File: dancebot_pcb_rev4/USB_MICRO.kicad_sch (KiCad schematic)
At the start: 10 parts, among them IC1 CP2102N-A02-GQFN28R, J12 USB_B_Micro

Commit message: schematic ready for review!
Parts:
- J12: footprint Connector_USB:USB_Micro-B_Wuerth_629105150521 -> Connector_USB:USB_Micro-B_Amphenol_10118193-0002LF_Horizontal
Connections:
- net +3V3: now also C11.1
- net D+: no longer D303.1 (K), IC1.5 (D-), J12.2 (D-)
- new net D-: D303.1 (K), IC1.5 (D-), J12.2 (D-)
- no-connect marks 16 -> 17
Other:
- note added: "Hierarchical Labels"
- moved on the sheet: C10, C11, D1, D3, D303, IC1, J12, R12, R7, R8

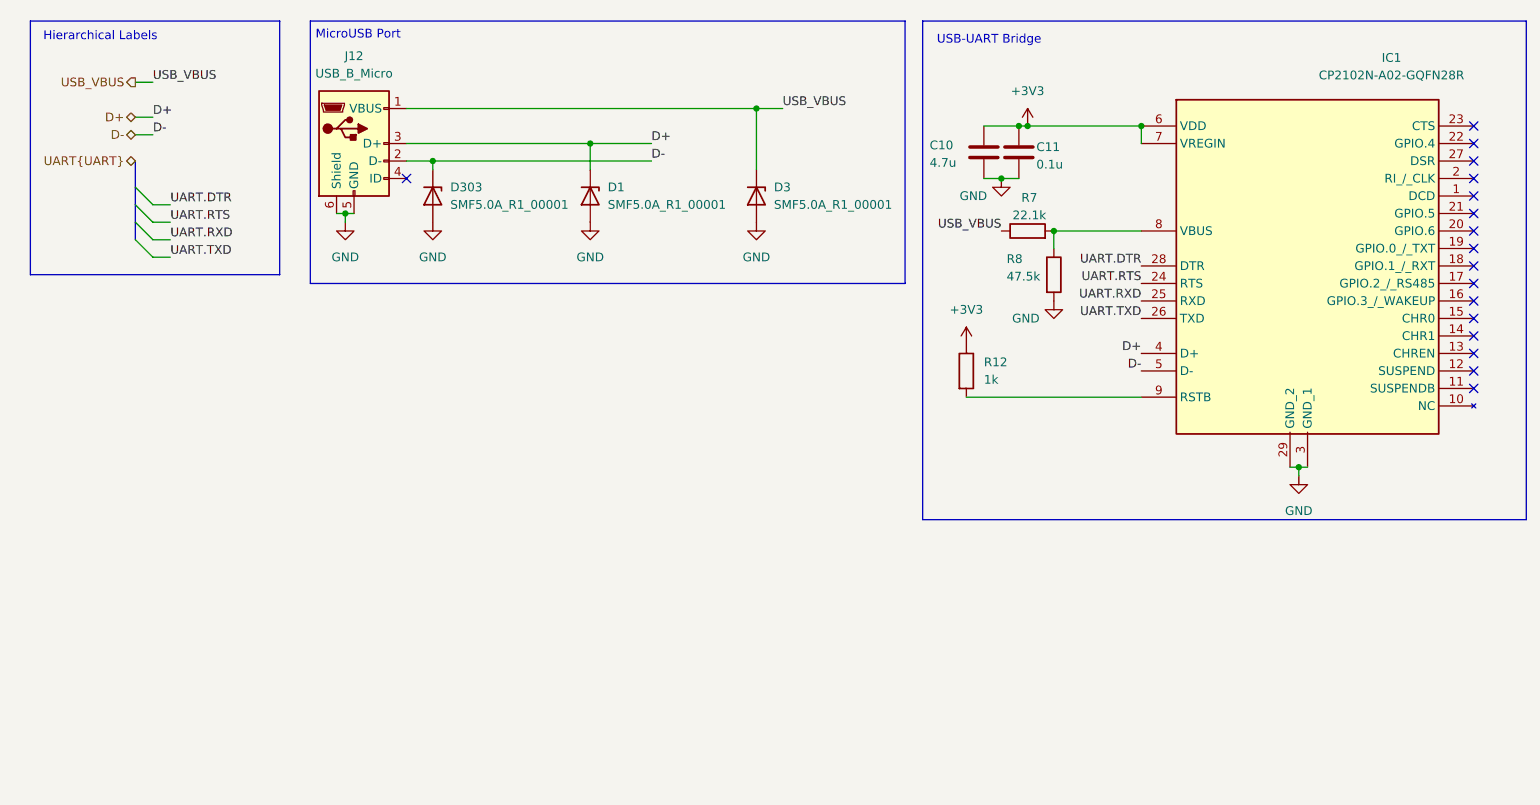
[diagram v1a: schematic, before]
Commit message: now using ESP32-S3-WROOM-1, changed power delivery system
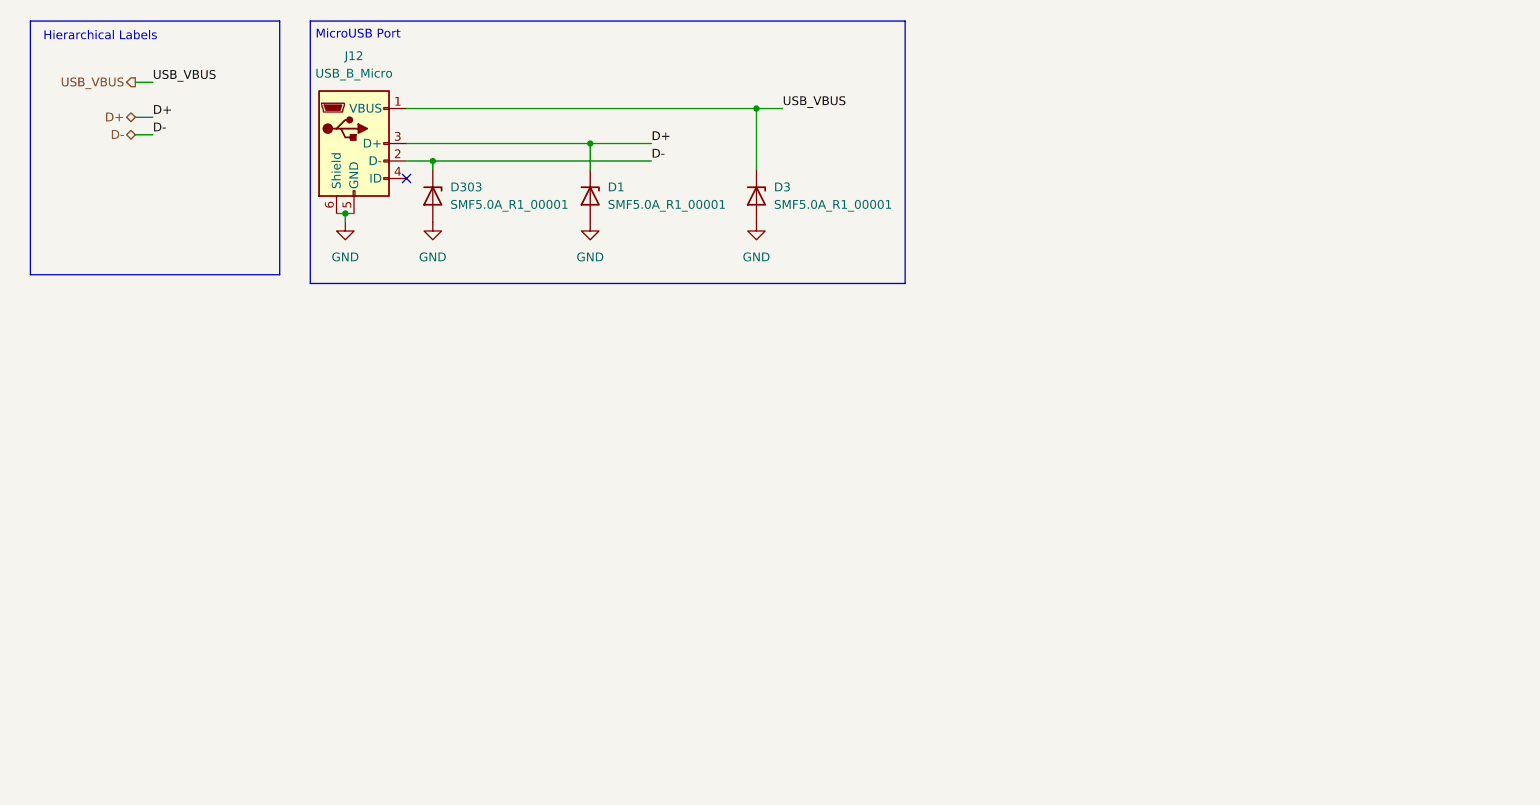
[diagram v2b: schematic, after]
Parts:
- removed C10: 4.7u, SamacSys_Parts:CAPC2013X140N, symbol Device:C
- removed C11: 0.1u, SamacSys_Parts:MAJx16, symbol Device:C
- removed IC1: CP2102N-A02-GQFN28R, SamacSys_Parts:QFN50P500X500X80-29N-D, symbol SamacSys_Parts:CP2102N-A02-GQFN28R
- removed R12: 1k, SamacSys_Parts:RESC2012X60N, symbol Device:R
- removed R7: 22.1k, SamacSys_Parts:RESC2012X50N, symbol Device:R
- removed R8: 47.5k, SamacSys_Parts:RESC2012X60N, symbol Device:R
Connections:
- no-connect marks 17 -> 1
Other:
- note removed: "USB-UART Bridge"

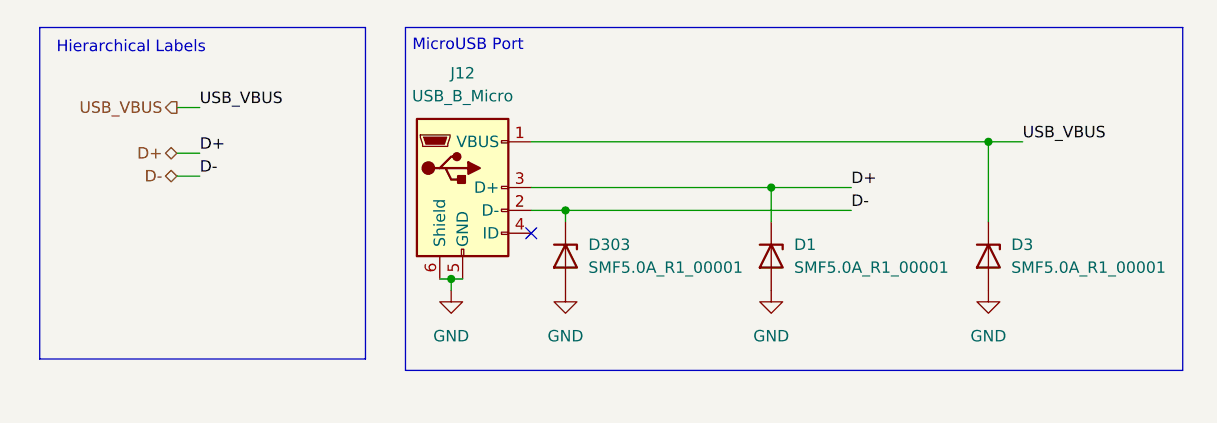
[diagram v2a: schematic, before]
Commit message: added more power leds. need to finish routing. fixed 3d models
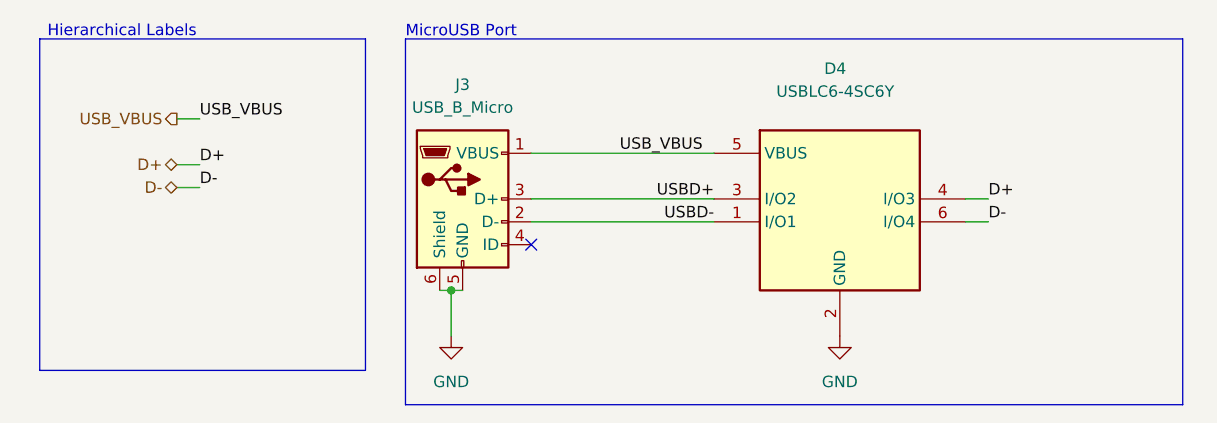
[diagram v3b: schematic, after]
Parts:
- removed D1, D3, D303: SMF5.0A_R1_00001, SamacSys_Parts:SMF50A_R1_00001, symbol Device:D_Zener
- added D4: USBLC6-4SC6Y, SamacSys_Parts:SOT95P280X145-6N, symbol SamacSys_Parts:USBLC6-4SC6Y
- renumbered J12 to J3
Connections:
- net D+: now also D4.4 (I/O3); no longer J3.3 (D+)
- net D-: now also D4.6 (I/O4); no longer J3.2 (D-)
- net GND: now also D4.2 (GND)
- net USB_VBUS: now also D4.5 (VBUS)
- new net USBD+: D4.3 (I/O2), J3.3 (D+)
- new net USBD-: D4.1 (I/O1), J3.2 (D-)
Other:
- moved on the sheet: J3

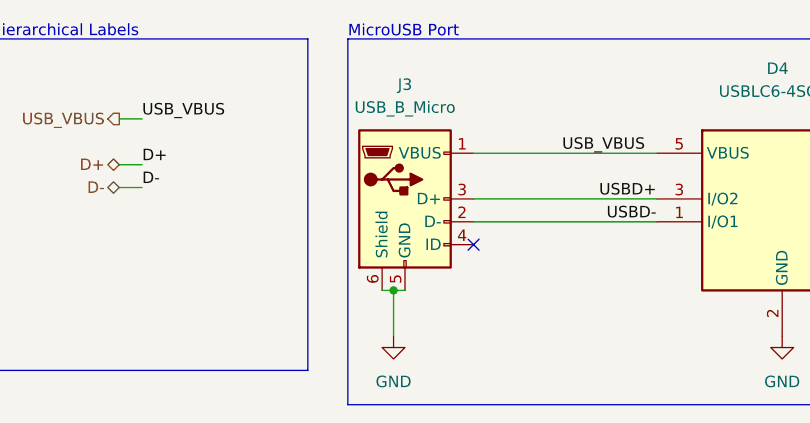
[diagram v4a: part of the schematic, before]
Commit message: moved some more stuff around. added gerbers
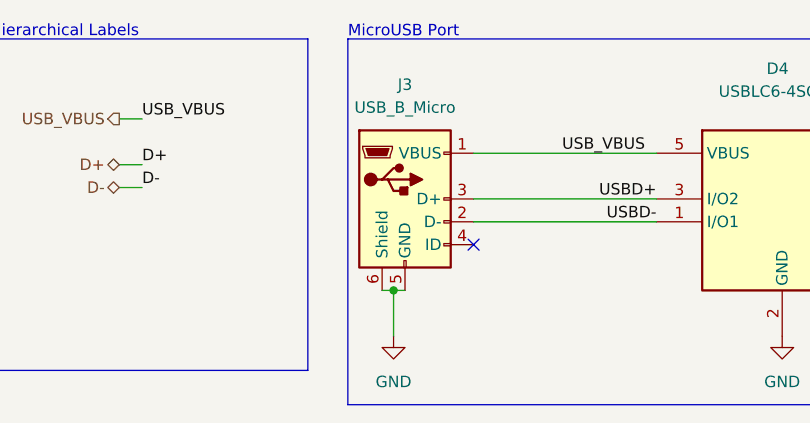
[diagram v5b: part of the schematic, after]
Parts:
- J3: symbol Connector:USB_B_Micro -> SamacSys_Parts:USB_B_Micro
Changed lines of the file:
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@@
 	)
 	(symbol
-		(lib_id "Connector:USB_B_Micro")
+		(lib_id "SamacSys_Parts:USB_B_Micro")
 		(at 60.96 33.02 0)
 		(unit 1)

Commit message: search replaced mouser.co.uk with mouser.com
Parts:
- D4: Mouser Price/Stock https://www.mouser.co.uk/ProductDetail/STMicroelectronics/U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 -> https://www.mouser.com/ProductDetail/STMicroelectronics/USB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
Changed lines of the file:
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@@
 			)
 		)
-		(property "Mouser Price/Stock" "https://www.mouser.co.uk/ProductDetail/STMicroelectronics/USBLC6-4SC6Y?qs=gNDSiZmRJS%252B5K%252Bxjl%252Bw9xw%3D%3D"
+		(property "Mouser Price/Stock" "https://www.mouser.com/ProductDetail/STMicroelectronics/USBLC6-4SC6Y?qs=gNDSiZmRJS%252B5K%252Bxjl%252Bw9xw%3D%3D"
 			(at 113.03 630.48 0)
 			(effects
